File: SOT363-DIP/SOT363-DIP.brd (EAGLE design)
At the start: 8.3 x 13.3 mm, 2 parts, among them Q1 2N7002DW

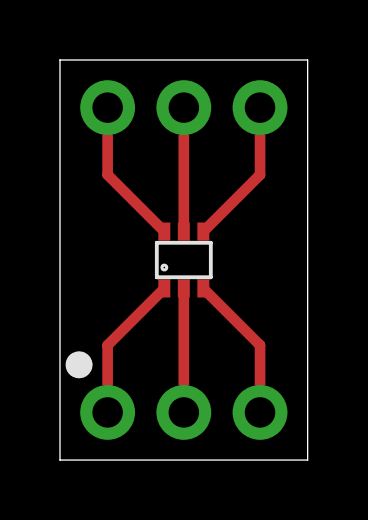
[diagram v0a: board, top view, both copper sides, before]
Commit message: sot23 + (soic8 & sot363 fix)
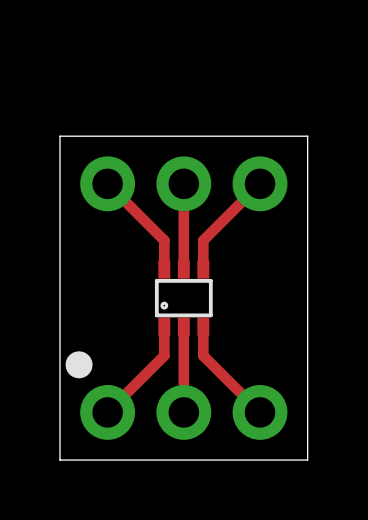
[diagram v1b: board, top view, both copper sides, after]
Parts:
- moved Q1 1.27 mm to (4.13, 5.40)
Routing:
- net N$2: track 4.13 -> 2.86 mm
- net N$6: track 4.91 -> 3.64 mm
- net N$5: track 4.13 -> 2.86 mm
- net N$4: track 4.91 -> 3.64 mm
- net N$3: track 4.91 -> 3.64 mm
- net N$1: track 4.91 -> 3.64 mm
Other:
- board size 8.3 x 13.3 mm -> 8.3 x 10.8 mm
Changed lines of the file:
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@@
 <?xml version="1.0" encoding="utf-8"?>
 <!DOCTYPE eagle SYSTEM "eagle.dtd">
-<eagle version="8.4.3">
+<eagle version="8.5.2">
 <drawing>
 <settings>
@@
 <setting verticaltext="up"/>
 </settings>
-<grid distance="12.5" unitdist="mil" unit="mil" style="lines" multiple="1" display="yes" altdistance="5" altunitdist="mil" altunit="mil"/>
+<grid distance="5" unitdist="mil" unit="mil" style="lines" multiple="1" display="yes" altdistance="5" altunitdist="mil" altunit="mil"/>
 <layers>
 <layer number="1" name="Top" color="4" fill="1" visible="yes" active="yes"/>
@@
 <board>
 <plain>
-<wire x1="0" y1="0" x2="0" y2="13.335" width="0" layer="20"/>
-<wire x1="0" y1="13.335" x2="8.255" y2="13.335" width="0" layer="20"/>
-<wire x1="8.255" y1="13.335" x2="8.255" y2="0" width="0" layer="20"/>
+<wire x1="0" y1="0" x2="0" y2="10.795" width="0" layer="20"/>
+<wire x1="0" y1="10.795" x2="8.255" y2="10.795" width="0" layer="20"/>
+<wire x1="8.255" y1="10.795" x2="8.255" y2="0" width="0" layer="20"/>
 <wire x1="8.255" y1="0" x2="0" y2="0" width="0" layer="20"/>
 </plain>
@@
 <param name="checkRestrict" value="0"/>
 <param name="checkStop" value="0"/>
+<param name="checkValues" value="0"/>
 <param name="useDiameter" value="13"/>
 <param name="maxErrors" value="50"/>
@@
 <elements>
 <element name="SOT-363" library="my-pinhead" package="ADAPTER-6" value="ADAPTER-6" x="0" y="0" smashed="yes">
-<attribute name="NAME" x="4.1275" y="6.6675" size="1.143" layer="22" ratio="16" rot="MR0" align="center"/>
+<attribute name="NAME" x="4.1275" y="5.3975" size="1.143" layer="22" ratio="16" rot="MR0" align="center"/>
 </element>
-<element name="Q1" library="my-mosfet" package="SOT363" value="2N7002DW" x="4.1275" y="6.6675" smashed="yes"/>
+<element name="Q1" library="my-mosfet" package="SOT363" value="2N7002DW" x="4.1275" y="5.3975" smashed="yes"/>
 </elements>
 <signals>
@@
 <contactref element="SOT-363" pad="6"/>
 <contactref element="Q1" pad="6"/>
-<wire x1="3.4775" y1="7.6175" x2="1.5875" y2="9.5075" width="0.3556" layer="1"/>
-<wire x1="1.5875" y1="9.5075" x2="1.5875" y2="11.7475" width="0.3556" layer="1"/>
+<wire x1="1.5875" y1="9.2075" x2="3.4775" y2="7.3175" width="0.3556" layer="1"/>
+<wire x1="3.4775" y1="7.3175" x2="3.4775" y2="6.3475" width="0.3556" layer="1"/>
 </signal>
 <signal name="N$6">
 <contactref element="SOT-363" pad="4"/>
 <contactref element="Q1" pad="4"/>
-<wire x1="4.7775" y1="7.6175" x2="6.6675" y2="9.5075" width="0.3556" layer="1"/>
-<wire x1="6.6675" y1="9.5075" x2="6.6675" y2="11.7475" width="0.3556" layer="1"/>
+<wire x1="6.6675" y1="9.2075" x2="4.7775" y2="7.3175" width="0.3556" layer="1"/>
+<wire x1="4.7775" y1="7.3175" x2="4.7775" y2="6.3475" width="0.3556" layer="1"/>
 </signal>
 <signal name="N$1">
 <contactref element="Q1" pad="3"/>
 <contactref element="SOT-363" pad="3"/>
-<wire x1="4.7775" y1="5.7175" x2="6.6675" y2="3.8275" width="0.3556" layer="1"/>
-<wire x1="6.6675" y1="3.8275" x2="6.6675" y2="1.5875" width="0.3556" layer="1"/>
+<wire x1="6.6675" y1="1.5875" x2="4.7775" y2="3.4775" width="0.3556" layer="1"/>
+<wire x1="4.7775" y1="3.4775" x2="4.7775" y2="4.4475" width="0.3556" layer="1"/>
 </signal>
 <signal name="N$3">
 <contactref element="SOT-363" pad="1"/>
 <contactref element="Q1" pad="1"/>
-<wire x1="3.4775" y1="5.7175" x2="1.5875" y2="3.8275" width="0.3556" layer="1"/>
-<wire x1="1.5875" y1="3.8275" x2="1.5875" y2="1.5875" width="0.3556" layer="1"/>
+<wire x1="1.5875" y1="1.5875" x2="3.4775" y2="3.4775" width="0.3556" layer="1"/>
+<wire x1="3.4775" y1="3.4775" x2="3.4775" y2="4.4475" width="0.3556" layer="1"/>
 </signal>
 <signal name="N$2">
 <contactref element="Q1" pad="5"/>
 <contactref element="SOT-363" pad="5"/>
-<wire x1="4.1275" y1="7.6175" x2="4.1275" y2="11.7475" width="0.3556" layer="1"/>
+<wire x1="4.1275" y1="6.3475" x2="4.1275" y2="9.2075" width="0.3556" layer="1"/>
 </signal>
 <signal name="N$5">
 <contactref element="Q1" pad="2"/>
 <contactref element="SOT-363" pad="2"/>
-<wire x1="4.1275" y1="1.5875" x2="4.1275" y2="5.7175" width="0.3556" layer="1"/>
+<wire x1="4.1275" y1="1.5875" x2="4.1275" y2="4.4475" width="0.3556" layer="1"/>
 </signal>
 </signals>
